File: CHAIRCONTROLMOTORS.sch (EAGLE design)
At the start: 51 parts, among them IC5 MCP2551, IC6 MCP2515, IC7 ATMEGA32U4NT, J1 LEFT MOTOR, J10 XTXX-30F, J11 USB-B-PTH, J12 M02X3-PIN, J2 RIGHT MOTOR, J3 M01-1.6MM, J4 M01-1.6MM, J5 M01-1.6MM, J6 M01-1.6MM, J7 M01-1.6MM, J8 M01-1.6MM, J9 XTXX-30F

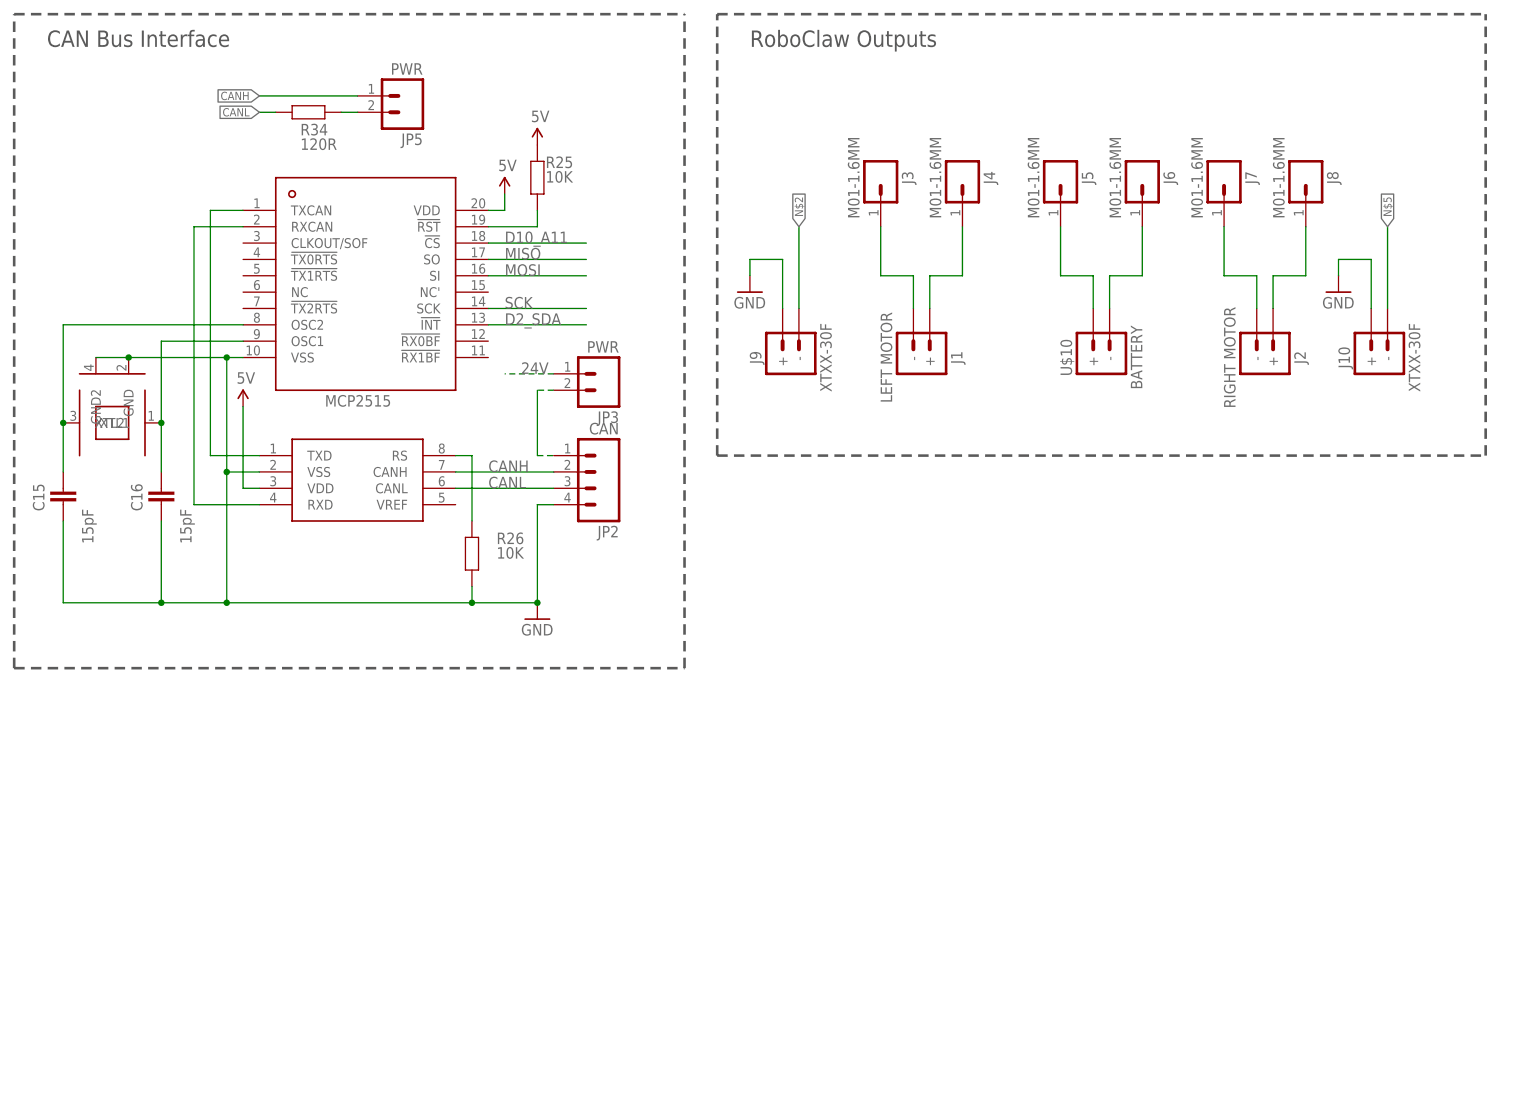
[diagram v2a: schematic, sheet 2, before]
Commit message: Schematic cleanups and start of placement
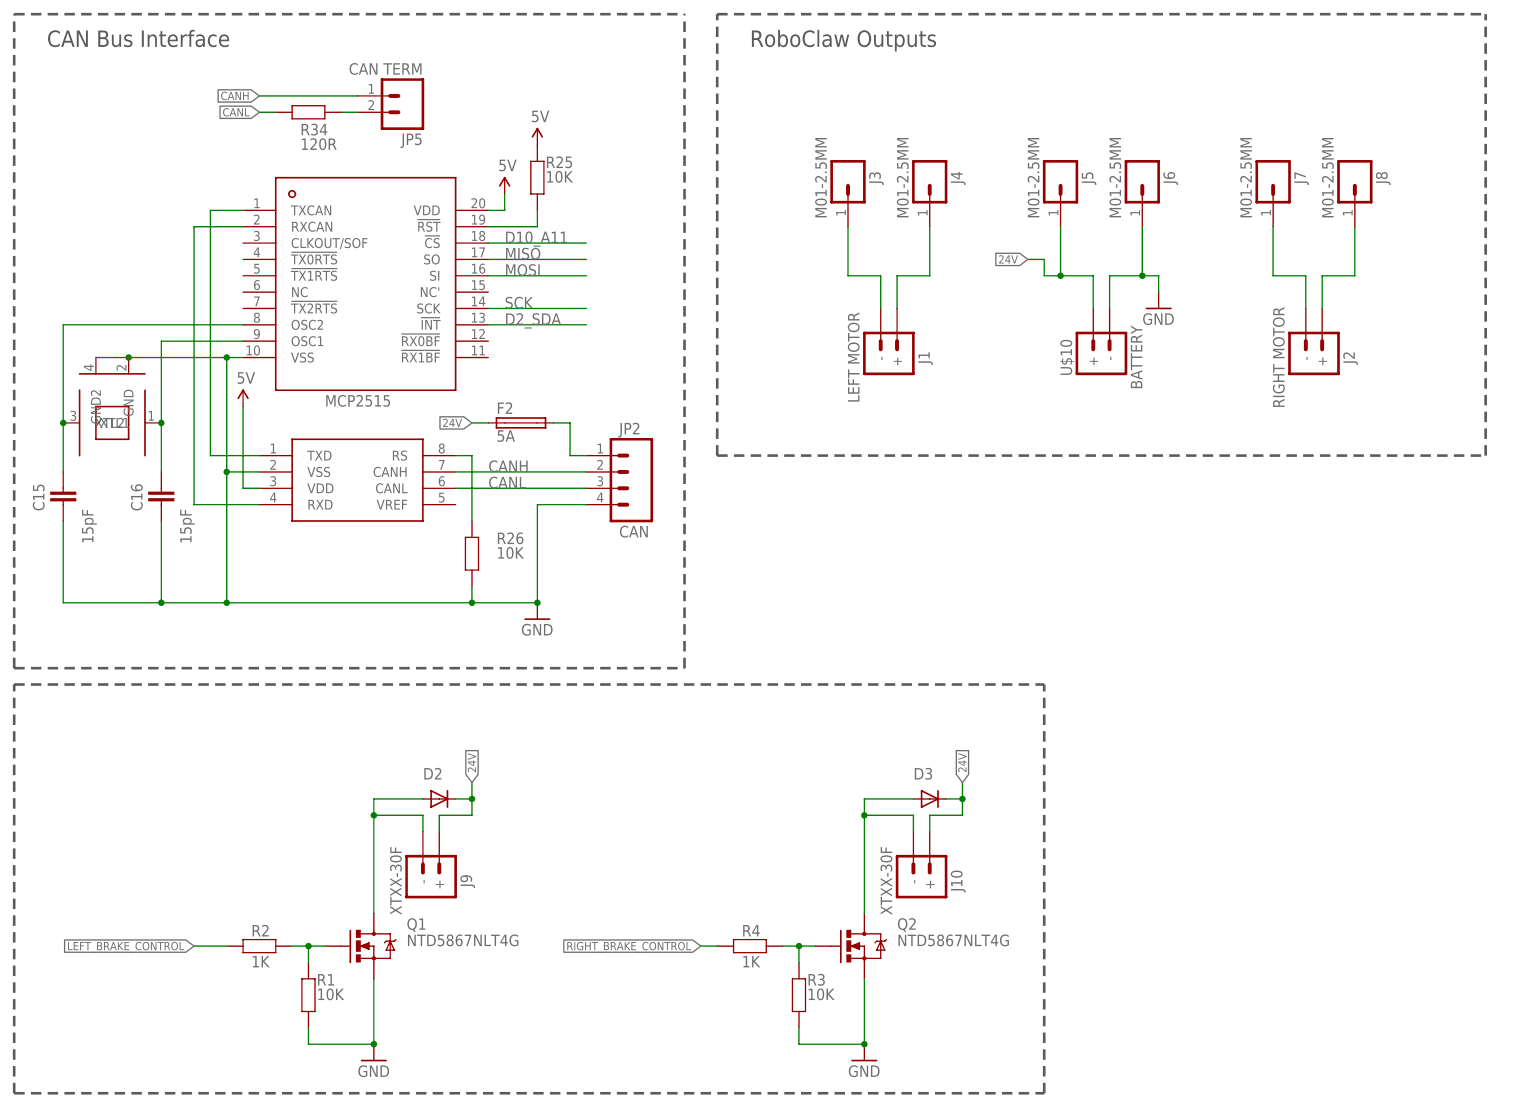
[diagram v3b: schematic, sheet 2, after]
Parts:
- removed JP3: PWR, freetronics-jon:M02PTH
- removed JP4: PWR, freetronics-jon:M03PTH
- removed REG1: K7805-500R3, freetronics-jon:K78XX-500R3
- added D2, D3: (no value), SuperHouse-DiscreteSemi:DIODESMA
- added F1: 500mA PTC 1812, SuperHouse-Fuses:PTC050
- added Q1, Q2: NTD5867NLT4G, SuperHouse-DiscreteSemi:MOSFET-NCHANNEL-DPAK
- added R1, R3: 10K, SuperHouse-DiscreteSemi:RESISTOR0603
- added R2, R4: 1K, SuperHouse-DiscreteSemi:RESISTOR0603
- C10, C11, C15, C16, C3, C7, C8, C9: device freetronics-master-v1.1:CAP0603 -> SuperHouse-DiscreteSemi:CAP0603
- D1: value 1N4004 -> SS56; device freetronics-jon:DIODESMB -> SuperHouse-DiscreteSemi:DIODESMA
- F2: value 500mA PTC 1812 -> 5A; device rcl:L-EUL1812 -> SuperHouse-Fuses:FUSE
- IC5: device freetronics-original:MCP2551 -> SuperHouse-ICs:MCP2551
- IC6: device MCP2515:MCP2515 -> SuperHouse-ICs:MCP2515
- IC7: value ATMEGA32U4NT -> ATMEGA32U4NT-TQFP; device freetronics-jon:ATMEGA32U4NT -> SuperHouse-MCUs:ATMEGA32U4NT-TQFP
- J3, J4, J5, J6, J7, J8: value M01-1.6MM -> M01-2.5MM; device SuperHouse-Connectors:M01-1.6MM -> SuperHouse-Connectors:M01-2.5MM
- JP2: device freetronics-jon:M04PTH -> SuperHouse-Connectors:M04-PIN
- JP5: value PWR -> CAN TERM; device freetronics-jon:M02PTH -> SuperHouse-Connectors:M02-PIN
- LED5, LED6, LED7, LED8: device freetronics-jon:LED0603 -> SuperHouse-LEDs:LED0603
- R19, R25, R26, R34: device freetronics-master-v1.1:RESISTOR0603 -> SuperHouse-DiscreteSemi:RESISTOR0603
- R20, R21, R22, R23, R24, R33: device freetronics-jon:RESISTOR0603 -> SuperHouse-DiscreteSemi:RESISTOR0603
- S1: device freetronics-jon:TAC_SWITCH_2PINSMT -> SuperHouse-Switches:TAC_SWITCH_2PINSMT
- XTL2, XTL4: device freetronics-jon:CRYSTAL-GND3X2 -> SuperHouse-Oscillators:CRYSTAL-GND3X2
- Z1, Z2: device freetronics-master-v1.1:RESISTOR0603 -> SuperHouse-DiscreteSemi:TVS0603
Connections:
- removed net N$10: J5.1, U$10.+
- removed net N$13: J6.1, U$10.-
- removed net N$39: JP2.1, JP3.2
- removed net N$5: J10.-
- new net LEFT_BRAKE: D2.A, J9.-, Q1.D
- new net LEFT_BRAKE_CONTROL: R2.2
- new net N$1: Q1.G, R1.2, R2.1
- new net N$4: Q2.G, R3.2, R4.1
- new net N$7: J12.2
- new net N$8: J12.1
- new net RIGHT_BRAKE: D3.A, J10.-, Q2.D
- new net RIGHT_BRAKE_CONTROL: R4.2
- net 24V: now also D2.C, D3.C, F2.1, J10.+, J5.1, J9.+, U$10.+; no longer JP3.1, JP4.2, REG1.IN
- net 5V: now also F1.2, J12.3, J12.4; no longer F2.2, ICSP1.2, REG1.OUT
- net GND: now also J12.5, J12.6, J6.1, Q1.S, Q2.S, R1.1, R3.1, U$10.-; no longer J10.+, J9.+, JP4.1, REG1.GND
- net N$2: now also F2.2, JP2.1; no longer J9.-
- net N$40: now also F1.1; no longer F2.1
- net USB+: now also ICSP1.2
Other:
- note added: "5V power is supplied by the RoboClaw via the comms header. USB VIN and ICSP VIN are linked. Fabricate with 2oz copper to provide adequate current capacity for high power tracks."
- note added: "RoboClaw Comms / Power"
- moved on the sheet: D1, J1, J10, J12, J2, J3, J4, J7, J8, J9, JP2

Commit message: More routing
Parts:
- J12: value M02X3-PIN -> RoboClaw
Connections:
- removed net N$7: J12.2
- removed net N$8: J12.1
- net D8_A9: now also J12.1
- net D9_A10: now also J12.2
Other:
- note added: "D0: D1: D2: SPI INT D3: D4: D5: D6: D7: D8: RoboClaw S2 D9: RoboClaw S1 D10: CAN SPI CS D11: D13: LED"
- note added: "S1"
- note added: "S2"

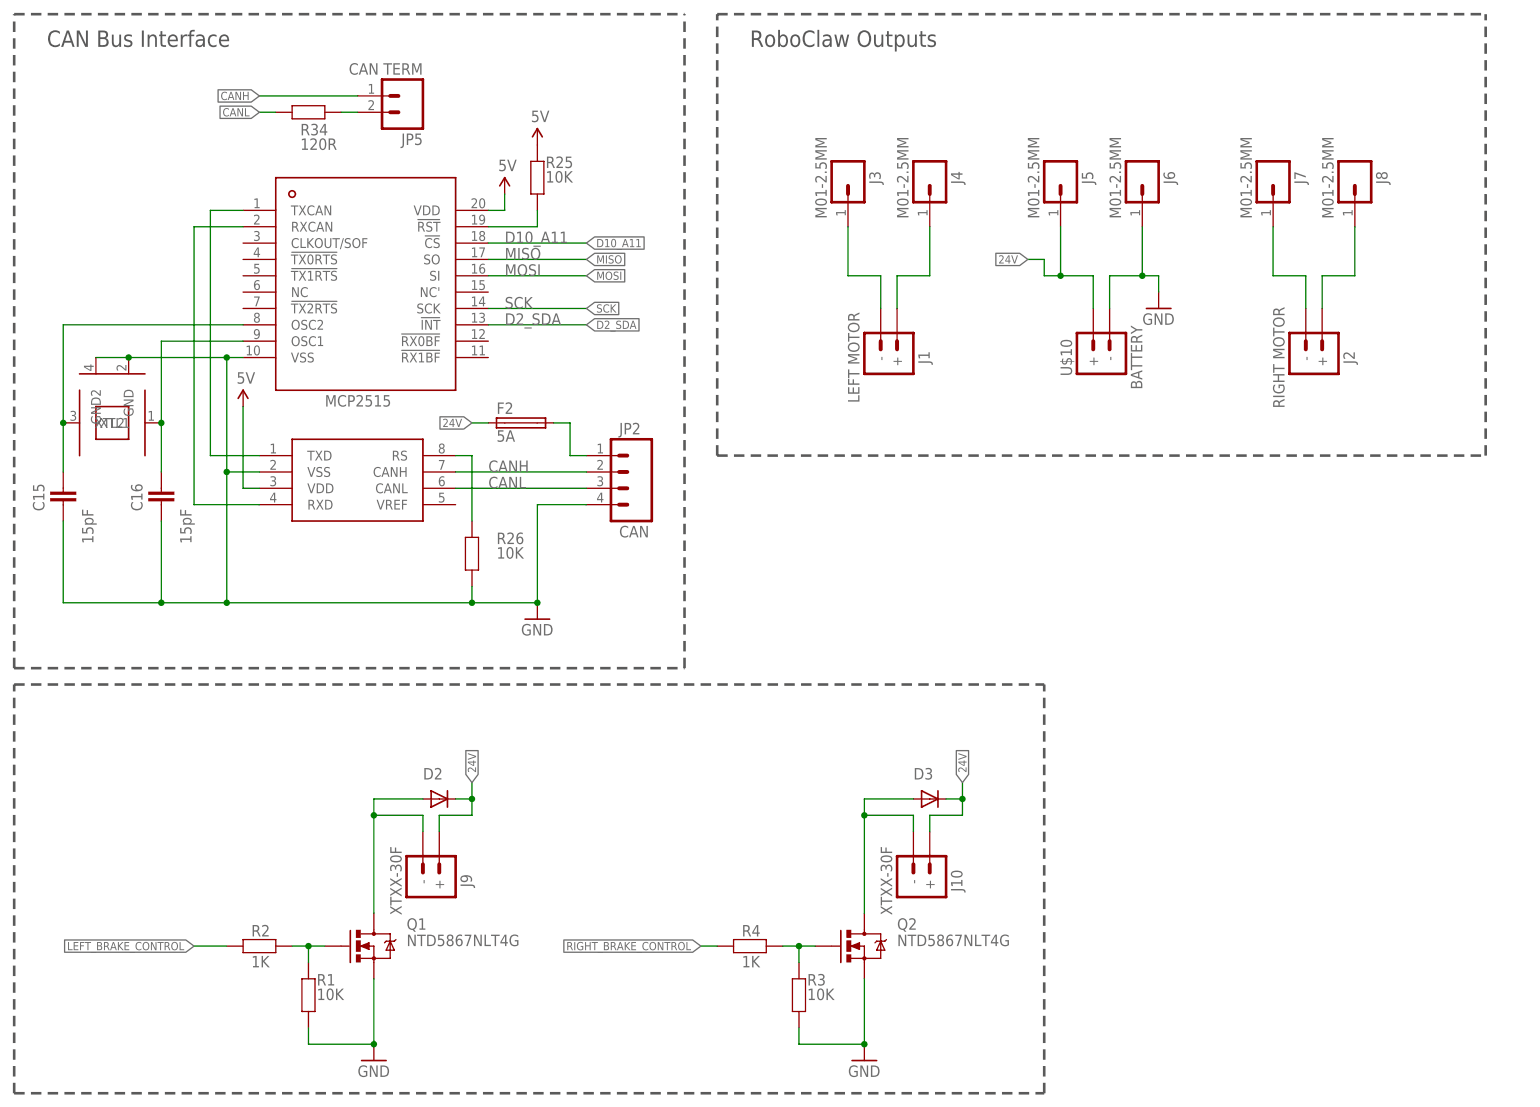
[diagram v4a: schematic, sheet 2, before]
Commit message: Added brake status detection, finished routing
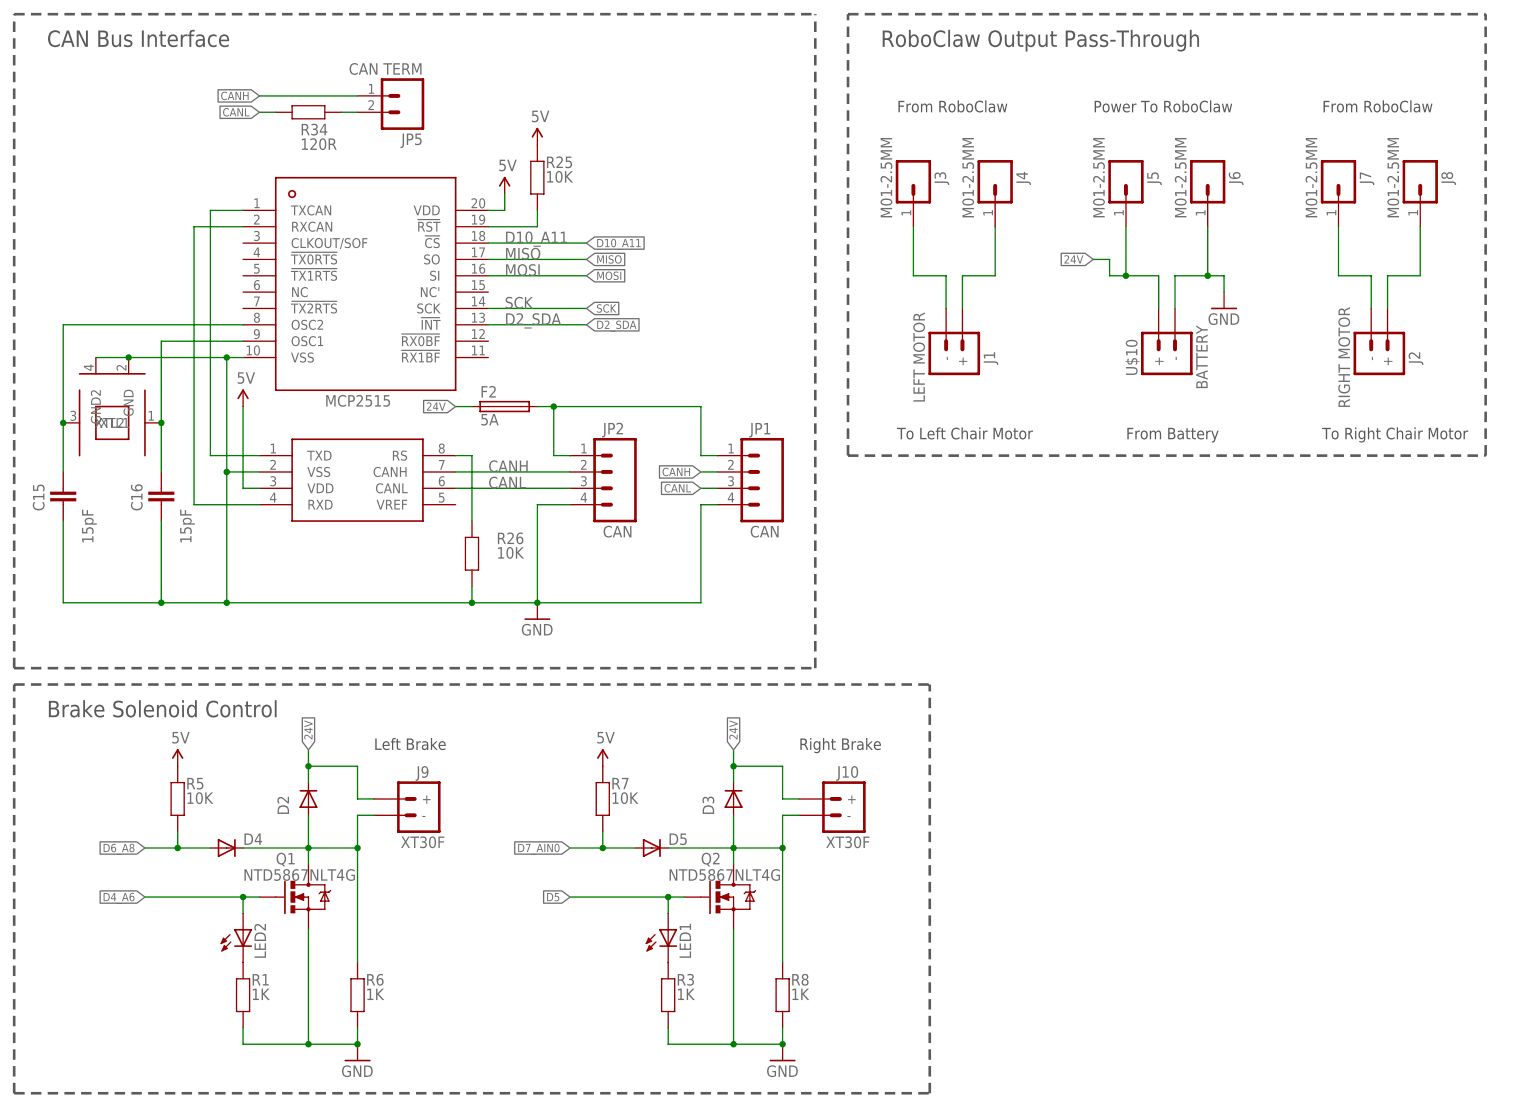
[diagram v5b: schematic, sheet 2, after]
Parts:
- removed ICSP1: ICSP, pinhead:PINHD-2X3
- removed R2, R4: 1K, SuperHouse-DiscreteSemi:RESISTOR0603
- added D4, D5: (no value), SuperHouse-DiscreteSemi:DIODESOD
- added JP1: CAN, SuperHouse-Connectors:M04-PIN
- added LED1, LED2: (no value), SuperHouse-LEDs:LED0603
- added R5, R7: 10K, SuperHouse-DiscreteSemi:RESISTOR0603
- added R6, R8: 1K, SuperHouse-DiscreteSemi:RESISTOR0603
- added U$6: ICSP-PIN, SuperHouse-Connectors:ICSP-PIN
- J10, J9: value XTXX-30F -> XT30F
- R1, R3: value 10K -> 1K
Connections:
- removed net LEFT_BRAKE_CONTROL: R2.2
- removed net N$4: Q2.G, R3.2, R4.1
- removed net RIGHT_BRAKE_CONTROL: R4.2
- new net N$5: LED1.C, R3.2
- net 5V: now also R5.2, R7.2
- net CANH: now also JP1.2
- net CANL: now also JP1.3
- net D4_A6: now also LED2.A, Q1.G
- net D5: now also LED1.A, Q2.G
- net D6_A8: now also D4.A, R5.1
- net D7_AIN0: now also D5.A, R7.1
- net GND: now also JP1.4, R6.1, R8.1, U$6.6; no longer ICSP1.6
- net LEFT_BRAKE: now also D4.C, R6.2
- net MISO: now also U$6.1; no longer ICSP1.1
- net MOSI: now also U$6.4; no longer ICSP1.4
- net N$1: now also LED2.C; no longer Q1.G, R2.1
- net N$2: now also JP1.1
- net RESET: now also U$6.5; no longer ICSP1.5
- net RIGHT_BRAKE: now also D5.C, R8.2
- net SCK: now also U$6.3; no longer ICSP1.3
- net USB+: now also U$6.2; no longer ICSP1.2
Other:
- note added: "Brake Solenoid Control"
- note added: "D0: D1: D2: SPI INT D3: D4: Left brake control D5: Right brake control D6: Left brake sensor D7: Right brake sensor D8: RoboClaw S2 D9: RoboClaw S1 D10: CAN SPI CS D11: D13: LED"
- note added: "From Battery"
- note added: "From RoboClaw"
- note added: "Left Brake"
- note added: "Power To RoboClaw"
- note added: "Right Brake"
- note added: "RoboClaw Output Pass-Through"
- note added: "To Do: * Sub-board to jumper to RoboClaw"
- note added: "To Left Chair Motor"
- note added: "To Right Chair Motor"
- note removed: "D0: D1: D2: SPI INT D3: D4: D5: D6: D7: D8: RoboClaw S2 D9: RoboClaw S1 D10: CAN SPI CS D11: D13: LED"
- note removed: "RoboClaw Outputs"
- note removed: "To Do: * Brake solenoid control with MOSFETs * Headers for interface with Roboclaw. D10/D11? * Circuit to detect brake switch position * Supply 24V to CAN connector * Headers for jumpers to RoboClaw * Sub-board to jumper to RoboClaw"
- moved on the sheet: D2, D3, F2, J1, J10, J2, J3, J4, J5, J6, J7, J8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
